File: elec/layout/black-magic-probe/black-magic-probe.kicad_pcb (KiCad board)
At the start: 2 copper layers, 48.1 x 19.2 mm, 61 parts

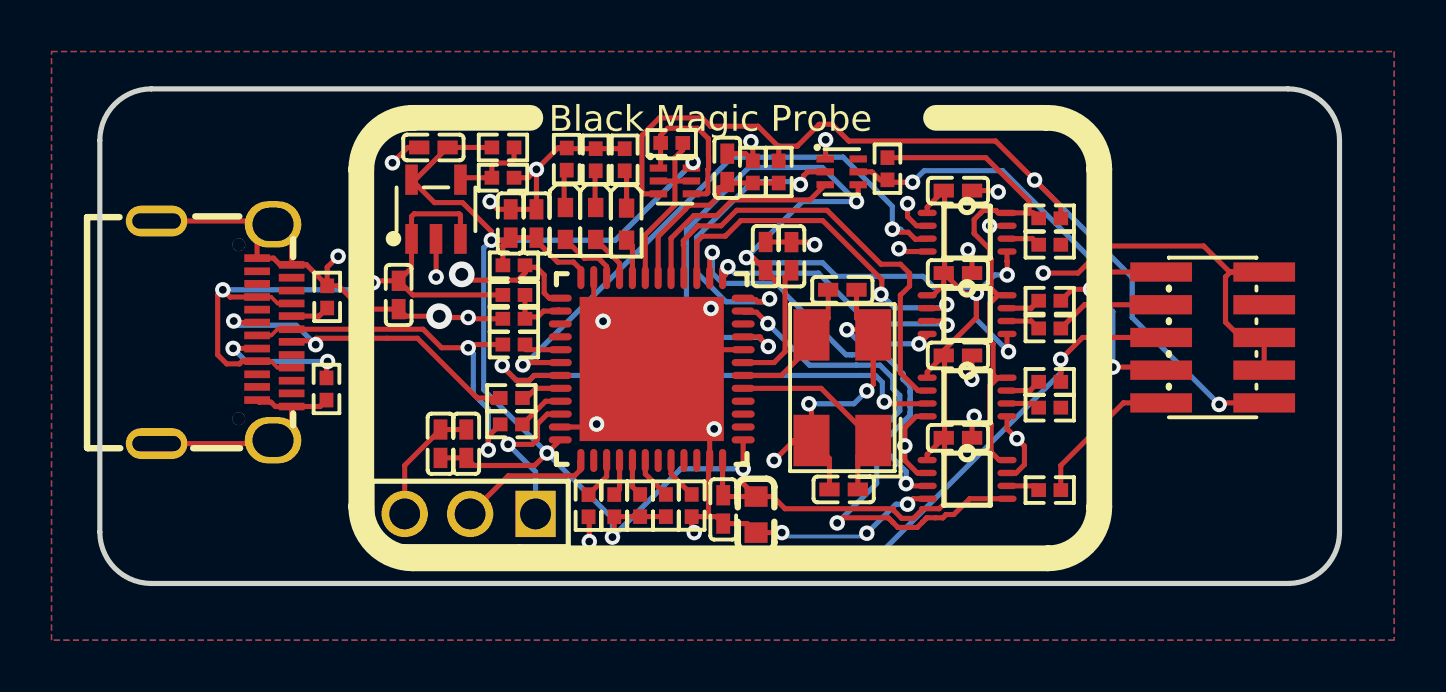
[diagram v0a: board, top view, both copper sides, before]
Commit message: Build everything with ordered params to fix frozen builds
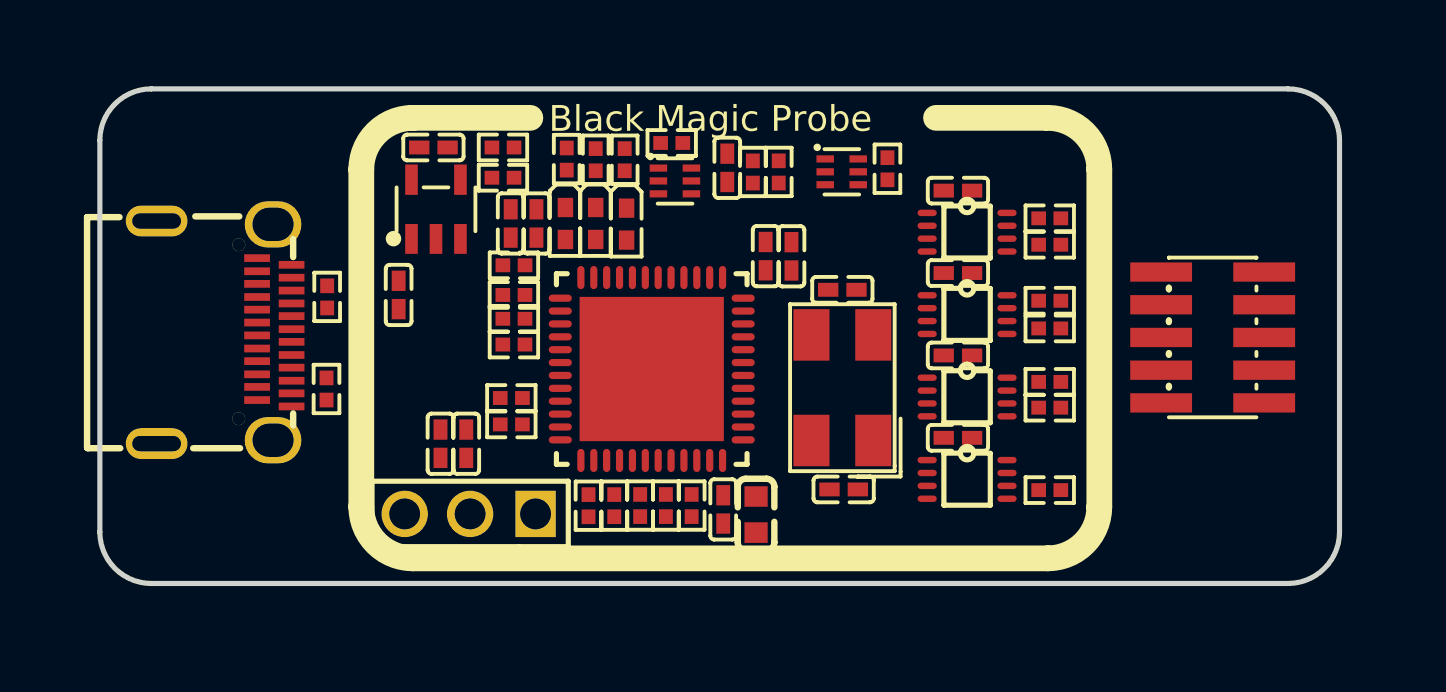
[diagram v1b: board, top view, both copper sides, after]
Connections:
- net CC1 renamed A5
- net G2 renamed black_magic_debugger-G2-1
- net black_magic_debugger-G1 renamed black_magic_debugger-G2
- net usb_connector.connector-B2 renamed SSTXP2
- C1 pad 1: hv-1 -> hv
- C10 pad 1: hv-1 -> hv
- C11 pad 1: hv-1 -> hv
- C15 pad 1: black_magic_debugger-line -> black_magic_debugger-line-4
- C16 pad 1: hv-2 -> hv-1
- C17 pad 1: hv-1 -> hv
- C2 pad 1: hv-1 -> hv
- C3 pad 1: hv-1 -> hv
- C4 pad 1: hv-1 -> hv
- C5 pad 1: hv-1 -> hv
- C6 pad 1: hv-1 -> hv
- C7 pad 1: hv-1 -> hv
- C8 pad 1: hv-1 -> hv
- C9 pad 1: hv-1 -> hv
- D1 pad 1: black_magic_debugger-anode-2 -> black_magic_debugger-anode-1
- D2 pad 1: black_magic_debugger-anode-1 -> black_magic_debugger-anode-2
- R1 pad 2: hv-1 -> hv
- R10 pad 1: line-4 -> line-3
- R11 pad 2: hv-1 -> hv
- R15 pad 1: black_magic_debugger-B2-1 -> black_magic_debugger-B2-3
- R15 pad 2: line-5 -> line-2
- R16 pad 2: line-2 -> line-4
- R17 pad 2: line -> line-5
- R18 pad 2: line-2 -> line-4
- R19 pad 1: black_magic_debugger-B2-3 -> black_magic_debugger-B2-2
- R19 pad 2: black_magic_debugger-line-4 -> black_magic_debugger-line-9
- R2 pad 2: hv-1 -> hv
- R20 pad 1: black_magic_debugger-B2-2 -> black_magic_debugger-B2-1
- R20 pad 2: black_magic_debugger-line-7 -> black_magic_debugger-line-6
- R21 pad 1: black_magic_debugger-line-2 -> black_magic_debugger-line-1
- R22 pad 1: hv-2 -> hv-1
- R22 pad 2: black_magic_debugger-line-2 -> black_magic_debugger-line-1
- R23 pad 1: black_magic_debugger-line -> black_magic_debugger-line-4
- R24 pad 1: hv -> hv-2
- R24 pad 2: black_magic_debugger-line -> black_magic_debugger-line-4
- R25 pad 2: hv -> hv-2
- R27 pad 1: hv-1 -> hv
- R3 pad 2: hv-1 -> hv
- R8 pad 1: line-4 -> line-3
- R9 pad 1: line-3 -> line
- U1 pad 1: hv-1 -> hv
- U1 pad 3: black_magic_debugger-line-9 -> black_magic_debugger-line-3
- U1 pad 5: hv-1 -> hv
- U1 pad 6: black_magic_debugger-B2-2 -> black_magic_debugger-B2-1
- U2 pad 1: hv-1 -> hv
- U2 pad 2: black_magic_debugger-line-8 -> black_magic_debugger-line-2
- U2 pad 5: hv-1 -> hv
- U2 pad 6: black_magic_debugger-B2-1 -> black_magic_debugger-B2-3
- U3 pad 1: hv-1 -> hv
- U3 pad 2: black_magic_debugger-line-6 -> black_magic_debugger-line
- U3 pad 3: black_magic_debugger-line-3 -> black_magic_debugger-line-7
- U3 pad 6: black_magic_debugger-B2-3 -> black_magic_debugger-B2-2
- U4 pad 1: hv-1 -> hv
- U4 pad 3: black_magic_debugger-line-1 -> black_magic_debugger-line-8
- U5 pad 1: hv-1 -> hv
- U5 pad 14: black_magic_debugger-line-1 -> black_magic_debugger-line-8
- U5 pad 15: black_magic_debugger-line-8 -> black_magic_debugger-line-2
- U5 pad 16: black_magic_debugger-line-6 -> black_magic_debugger-line
- U5 pad 18: black_magic_debugger-line -> black_magic_debugger-line-4
- U5 pad 20: black_magic_debugger-anode-2 -> black_magic_debugger-anode-1
- U5 pad 21: black_magic_debugger-anode-1 -> black_magic_debugger-anode-2
- U5 pad 24: hv-1 -> hv
- U5 pad 26: black_magic_debugger-line-2 -> black_magic_debugger-line-1
- U5 pad 30: black_magic_debugger-line-9 -> black_magic_debugger-line-3
- U5 pad 31: black_magic_debugger-line-3 -> black_magic_debugger-line-7
- U5 pad 36: hv-1 -> hv
- U5 pad 48: hv-1 -> hv
- U5 pad 9: hv-1 -> hv
- U6 pad 3: hv -> hv-2
- U6 pad 6: hv-1 -> hv
- U7 pad 4: hv-1 -> hv
- U8 pad 1: hv -> hv-2
- U8 pad 2: line -> line-5
- U8 pad 6: line-2 -> line-4
- U8 pad 8: line-5 -> line-2
- U9 pad 1: hv-2 -> hv-1
- U9 pad 3: hv-2 -> hv-1
- U9 pad 5: hv-1 -> hv
- USB1 pad A4: hv-2 -> hv-1
- USB1 pad A6: line-4 -> line-3
- USB1 pad A7: line-3 -> line
- USB1 pad A9: hv-2 -> hv-1
- USB1 pad B4: hv-2 -> hv-1
- USB1 pad B6: line-4 -> line-3
- USB1 pad B7: line-3 -> line
- USB1 pad B9: hv-2 -> hv-1
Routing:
- net gnd: track 133.6 -> 0.00 mm, vias 34 -> 0
- net hv-1: track 121.3 -> 0.00 mm, vias 11 -> 0
- net hv: track 36.1 -> 0.00 mm, vias 2 -> 0
- net line-2: track 28.0 -> 0.00 mm, vias 2 -> 0
- net hv-2: track 25.5 -> 0.00 mm, vias 2 -> 0
- net black_magic_debugger-line-9: track 22.8 -> 0.00 mm, vias 2 -> 0
- net VCCB: track 21.8 -> 0.00 mm
- net DIR: track 20.9 -> 0.00 mm, vias 2 -> 0
- net black_magic_debugger-line-3: track 20.3 -> 0.00 mm, vias 2 -> 0
- net black_magic_debugger-line-6: track 17.1 -> 0.00 mm
- net black_magic_debugger-line-1: track 16.8 -> 0.00 mm, vias 2 -> 0
- net line-4: track 15.5 -> 0.00 mm, vias 2 -> 0
- net line-3: track 14.8 -> 0.00 mm, vias 2 -> 0
- net black_magic_debugger-line-8: track 14.1 -> 0.00 mm, vias 2 -> 0
- net G1: track 13.7 -> 0.00 mm, vias 2 -> 0
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- removed copper zone on B.Cu, net gnd
- removed copper zone on F.Cu, net gnd

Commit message: from testing, it doesnt work very well without traces
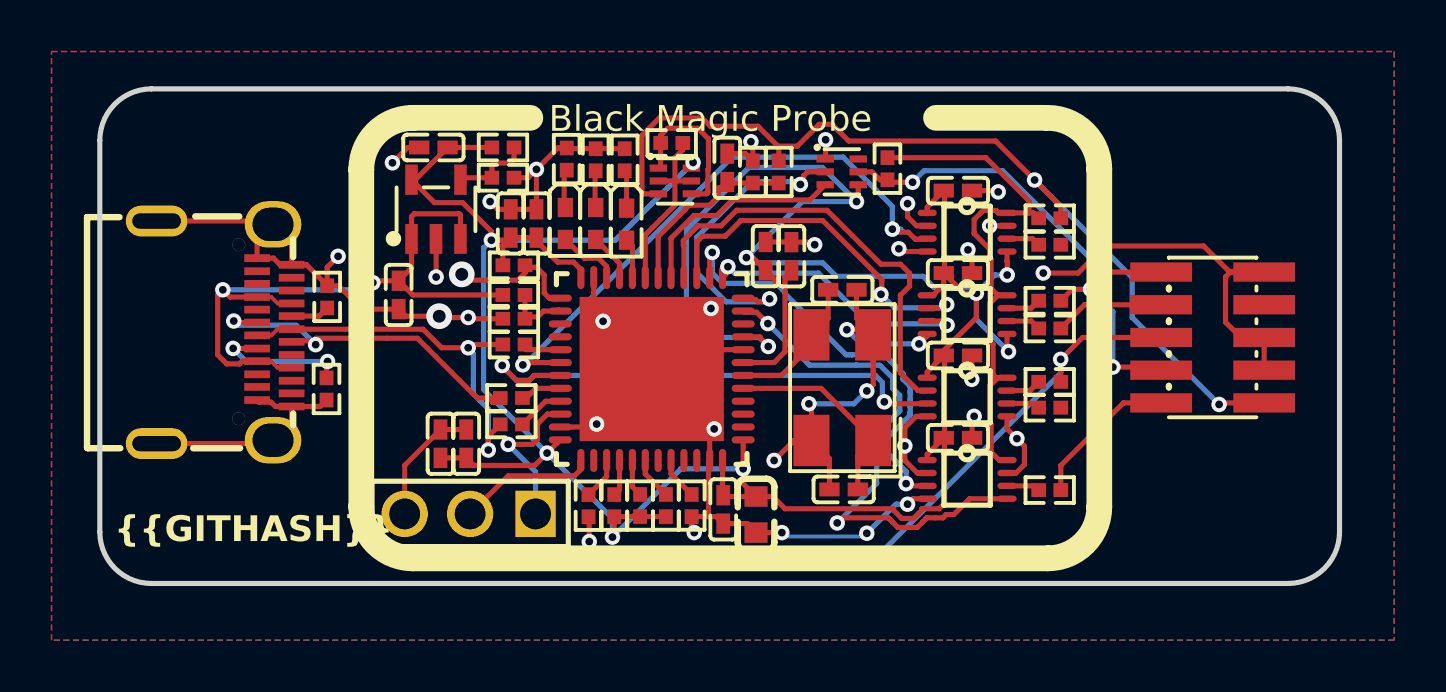
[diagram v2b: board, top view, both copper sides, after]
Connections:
- net A5 renamed CC1
- net SSTXP2 renamed usb_connector.connector-B2
- net black_magic_debugger-G2 renamed black_magic_debugger-G1
- net black_magic_debugger-G2-1 renamed G2
- C1 pad 1: hv -> hv-1
- C10 pad 1: hv -> hv-1
- C11 pad 1: hv -> hv-1
- C15 pad 1: black_magic_debugger-line-4 -> black_magic_debugger-line
- C16 pad 1: hv-1 -> hv-2
- C17 pad 1: hv -> hv-1
- C2 pad 1: hv -> hv-1
- C3 pad 1: hv -> hv-1
- C4 pad 1: hv -> hv-1
- C5 pad 1: hv -> hv-1
- C6 pad 1: hv -> hv-1
- C7 pad 1: hv -> hv-1
- C8 pad 1: hv -> hv-1
- C9 pad 1: hv -> hv-1
- D1 pad 1: black_magic_debugger-anode-1 -> black_magic_debugger-anode-2
- D2 pad 1: black_magic_debugger-anode-2 -> black_magic_debugger-anode-1
- R1 pad 2: hv -> hv-1
- R10 pad 1: line-3 -> line-4
- R11 pad 2: hv -> hv-1
- R15 pad 1: black_magic_debugger-B2-3 -> black_magic_debugger-B2-1
- R15 pad 2: line-2 -> line-5
- R16 pad 2: line-4 -> line-2
- R17 pad 2: line-5 -> line
- R18 pad 2: line-4 -> line-2
- R19 pad 1: black_magic_debugger-B2-2 -> black_magic_debugger-B2-3
- R19 pad 2: black_magic_debugger-line-9 -> black_magic_debugger-line-4
- R2 pad 2: hv -> hv-1
- R20 pad 1: black_magic_debugger-B2-1 -> black_magic_debugger-B2-2
- R20 pad 2: black_magic_debugger-line-6 -> black_magic_debugger-line-7
- R21 pad 1: black_magic_debugger-line-1 -> black_magic_debugger-line-2
- R22 pad 1: hv-1 -> hv-2
- R22 pad 2: black_magic_debugger-line-1 -> black_magic_debugger-line-2
- R23 pad 1: black_magic_debugger-line-4 -> black_magic_debugger-line
- R24 pad 1: hv-2 -> hv
- R24 pad 2: black_magic_debugger-line-4 -> black_magic_debugger-line
- R25 pad 2: hv-2 -> hv
- R27 pad 1: hv -> hv-1
- R3 pad 2: hv -> hv-1
- R8 pad 1: line-3 -> line-4
- R9 pad 1: line -> line-3
- U1 pad 1: hv -> hv-1
- U1 pad 3: black_magic_debugger-line-3 -> black_magic_debugger-line-9
- U1 pad 5: hv -> hv-1
- U1 pad 6: black_magic_debugger-B2-1 -> black_magic_debugger-B2-2
- U2 pad 1: hv -> hv-1
- U2 pad 2: black_magic_debugger-line-2 -> black_magic_debugger-line-8
- U2 pad 5: hv -> hv-1
- U2 pad 6: black_magic_debugger-B2-3 -> black_magic_debugger-B2-1
- U3 pad 1: hv -> hv-1
- U3 pad 2: black_magic_debugger-line -> black_magic_debugger-line-6
- U3 pad 3: black_magic_debugger-line-7 -> black_magic_debugger-line-3
- U3 pad 6: black_magic_debugger-B2-2 -> black_magic_debugger-B2-3
- U4 pad 1: hv -> hv-1
- U4 pad 3: black_magic_debugger-line-8 -> black_magic_debugger-line-1
- U5 pad 1: hv -> hv-1
- U5 pad 14: black_magic_debugger-line-8 -> black_magic_debugger-line-1
- U5 pad 15: black_magic_debugger-line-2 -> black_magic_debugger-line-8
- U5 pad 16: black_magic_debugger-line -> black_magic_debugger-line-6
- U5 pad 18: black_magic_debugger-line-4 -> black_magic_debugger-line
- U5 pad 20: black_magic_debugger-anode-1 -> black_magic_debugger-anode-2
- U5 pad 21: black_magic_debugger-anode-2 -> black_magic_debugger-anode-1
- U5 pad 24: hv -> hv-1
- U5 pad 26: black_magic_debugger-line-1 -> black_magic_debugger-line-2
- U5 pad 30: black_magic_debugger-line-3 -> black_magic_debugger-line-9
- U5 pad 31: black_magic_debugger-line-7 -> black_magic_debugger-line-3
- U5 pad 36: hv -> hv-1
- U5 pad 48: hv -> hv-1
- U5 pad 9: hv -> hv-1
- U6 pad 3: hv-2 -> hv
- U6 pad 6: hv -> hv-1
- U7 pad 4: hv -> hv-1
- U8 pad 1: hv-2 -> hv
- U8 pad 2: line-5 -> line
- U8 pad 6: line-4 -> line-2
- U8 pad 8: line-2 -> line-5
- U9 pad 1: hv-1 -> hv-2
- U9 pad 3: hv-1 -> hv-2
- U9 pad 5: hv -> hv-1
- USB1 pad A4: hv-1 -> hv-2
- USB1 pad A6: line-3 -> line-4
- USB1 pad A7: line -> line-3
- USB1 pad A9: hv-1 -> hv-2
- USB1 pad B4: hv-1 -> hv-2
- USB1 pad B6: line-3 -> line-4
- USB1 pad B7: line -> line-3
- USB1 pad B9: hv-1 -> hv-2
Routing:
- net gnd: track 0.00 -> 133.6 mm, vias 0 -> 34
- net hv-1: track 0.00 -> 121.3 mm, vias 0 -> 11
- net hv: track 0.00 -> 36.1 mm, vias 0 -> 2
- net line-2: track 0.00 -> 28.0 mm, vias 0 -> 2
- net hv-2: track 0.00 -> 25.5 mm, vias 0 -> 2
- net black_magic_debugger-line-9: track 0.00 -> 22.8 mm, vias 0 -> 2
- net VCCB: track 0.00 -> 21.8 mm
- net DIR: track 0.00 -> 20.9 mm, vias 0 -> 2
- net black_magic_debugger-line-3: track 0.00 -> 20.3 mm, vias 0 -> 2
- net black_magic_debugger-line-6: track 0.00 -> 17.1 mm
- net black_magic_debugger-line-1: track 0.00 -> 16.8 mm, vias 0 -> 2
- net line-4: track 0.00 -> 15.5 mm, vias 0 -> 2
- net line-3: track 0.00 -> 14.8 mm, vias 0 -> 2
- net black_magic_debugger-line-8: track 0.00 -> 14.1 mm, vias 0 -> 2
- net G1: track 0.00 -> 13.7 mm, vias 0 -> 2
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- added copper zone on B.Cu, net gnd
- added copper zone on F.Cu, net gnd
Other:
- board text added: "{{GITHASH}}"

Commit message: checkin
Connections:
- net CC1 renamed A5
- net G2 renamed black_magic_debugger-G2-1
- net black_magic_debugger-G1 renamed black_magic_debugger-G2
- C1 pad 1: hv-1 -> hv
- C10 pad 1: hv-1 -> hv
- C11 pad 1: hv-1 -> hv
- C15 pad 1: black_magic_debugger-line -> black_magic_debugger-line-3
- C17 pad 1: hv-1 -> hv
- C2 pad 1: hv-1 -> hv
- C3 pad 1: hv-1 -> hv
- C4 pad 1: hv-1 -> hv
- C5 pad 1: hv-1 -> hv
- C6 pad 1: hv-1 -> hv
- C7 pad 1: hv-1 -> hv
- C8 pad 1: hv-1 -> hv
- C9 pad 1: hv-1 -> hv
- D2 pad 1: black_magic_debugger-anode-1 -> black_magic_debugger-anode
- D3 pad 1: black_magic_debugger-anode -> black_magic_debugger-anode-1
- R1 pad 2: hv-1 -> hv
- R10 pad 1: line-4 -> line-3
- R11 pad 2: hv-1 -> hv
- R14 pad 2: line-1 -> line-4
- R15 pad 1: black_magic_debugger-B2-1 -> black_magic_debugger-B2-3
- R15 pad 2: line-5 -> line-2
- R16 pad 2: line-2 -> line-1
- R17 pad 1: black_magic_debugger-B2 -> black_magic_debugger-B2-2
- R18 pad 2: line-2 -> line-1
- R19 pad 1: black_magic_debugger-B2-3 -> black_magic_debugger-B2-1
- R19 pad 2: black_magic_debugger-line-4 -> black_magic_debugger-line-5
- R2 pad 2: hv-1 -> hv
- R20 pad 1: black_magic_debugger-B2-2 -> black_magic_debugger-B2
- R20 pad 2: black_magic_debugger-line-7 -> black_magic_debugger-line-8
- R21 pad 1: black_magic_debugger-line-2 -> black_magic_debugger-line
- R22 pad 2: black_magic_debugger-line-2 -> black_magic_debugger-line
- R23 pad 1: black_magic_debugger-line -> black_magic_debugger-line-3
- R24 pad 1: hv -> hv-1
- R24 pad 2: black_magic_debugger-line -> black_magic_debugger-line-3
- R25 pad 2: hv -> hv-1
- R27 pad 1: hv-1 -> hv
- R3 pad 2: hv-1 -> hv
- R8 pad 1: line-4 -> line-3
- R9 pad 1: line-3 -> line-5
- U1 pad 1: hv-1 -> hv
- U1 pad 5: hv-1 -> hv
- U1 pad 6: black_magic_debugger-B2-2 -> black_magic_debugger-B2
- U2 pad 1: hv-1 -> hv
- U2 pad 2: black_magic_debugger-line-8 -> black_magic_debugger-line-7
- U2 pad 3: black_magic_debugger-line-5 -> black_magic_debugger-line-4
- U2 pad 5: hv-1 -> hv
- U2 pad 6: black_magic_debugger-B2-1 -> black_magic_debugger-B2-3
- U3 pad 1: hv-1 -> hv
- U3 pad 2: black_magic_debugger-line-6 -> black_magic_debugger-line-2
- U3 pad 3: black_magic_debugger-line-3 -> black_magic_debugger-line-1
- U3 pad 6: black_magic_debugger-B2-3 -> black_magic_debugger-B2-1
- U4 pad 1: hv-1 -> hv
- U4 pad 3: black_magic_debugger-line-1 -> black_magic_debugger-line-6
- U4 pad 6: black_magic_debugger-B2 -> black_magic_debugger-B2-2
- U5 pad 1: hv-1 -> hv
- U5 pad 13: black_magic_debugger-line-5 -> black_magic_debugger-line-4
- U5 pad 14: black_magic_debugger-line-1 -> black_magic_debugger-line-6
- U5 pad 15: black_magic_debugger-line-8 -> black_magic_debugger-line-7
- U5 pad 16: black_magic_debugger-line-6 -> black_magic_debugger-line-2
- U5 pad 18: black_magic_debugger-line -> black_magic_debugger-line-3
- U5 pad 21: black_magic_debugger-anode-1 -> black_magic_debugger-anode
- U5 pad 22: black_magic_debugger-anode -> black_magic_debugger-anode-1
- U5 pad 24: hv-1 -> hv
- U5 pad 26: black_magic_debugger-line-2 -> black_magic_debugger-line
- U5 pad 31: black_magic_debugger-line-3 -> black_magic_debugger-line-1
- U5 pad 36: hv-1 -> hv
- U5 pad 48: hv-1 -> hv
- U5 pad 9: hv-1 -> hv
- U6 pad 3: hv -> hv-1
- U6 pad 6: hv-1 -> hv
- U7 pad 4: hv-1 -> hv
- U8 pad 1: hv -> hv-1
- U8 pad 4: line-1 -> line-4
- U8 pad 6: line-2 -> line-1
- U8 pad 8: line-5 -> line-2
- U9 pad 5: hv-1 -> hv
- USB1 pad A6: line-4 -> line-3
- USB1 pad A7: line-3 -> line-5
- USB1 pad B6: line-4 -> line-3
- USB1 pad B7: line-3 -> line-5
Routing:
- net hv-1: track 121.3 -> 36.1 mm, vias 11 -> 2
- net hv: track 36.1 -> 121.3 mm, vias 2 -> 11
- net line-2: track 28.0 -> 4.28 mm, vias 2 -> 0
- net line-1: track 6.64 -> 28.0 mm
- net black_magic_debugger-line-2: track 2.58 -> 17.1 mm
- net black_magic_debugger-line-8: track 14.1 -> 0.00 mm, vias 2 -> 0
- net black_magic_debugger-line-7: track 0.00 -> 14.1 mm, vias 0 -> 2
- net black_magic_debugger-line-3: track 20.3 -> 7.33 mm, vias 2 -> 0
- net black_magic_debugger-line-5: track 10.8 -> 0.00 mm, vias 2 -> 0
- net black_magic_debugger-line-4: track 0.00 -> 10.8 mm, vias 0 -> 2
- net line-5: track 4.28 -> 14.8 mm, vias 0 -> 2
- net line-4: track 15.5 -> 6.64 mm
- net black_magic_debugger-line: track 7.33 -> 2.58 mm
- net black_magic_debugger-line-1: track 16.8 -> 20.3 mm
- net line-3: track 14.8 -> 15.5 mm
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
